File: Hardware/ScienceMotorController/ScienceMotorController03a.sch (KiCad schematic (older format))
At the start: 16 parts

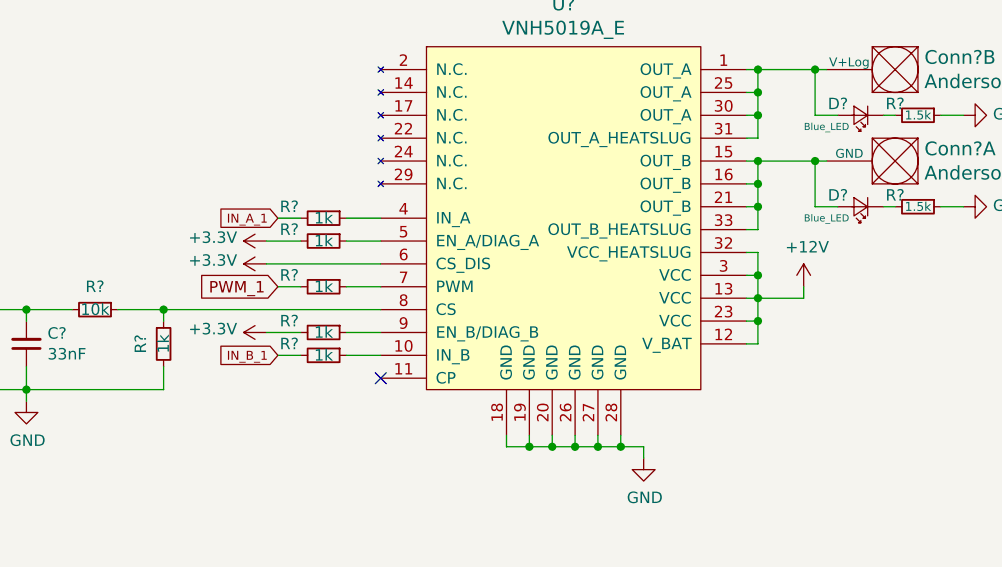
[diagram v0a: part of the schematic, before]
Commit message: changed everything to actuation, added schottky diode, added A/B flags to tiva
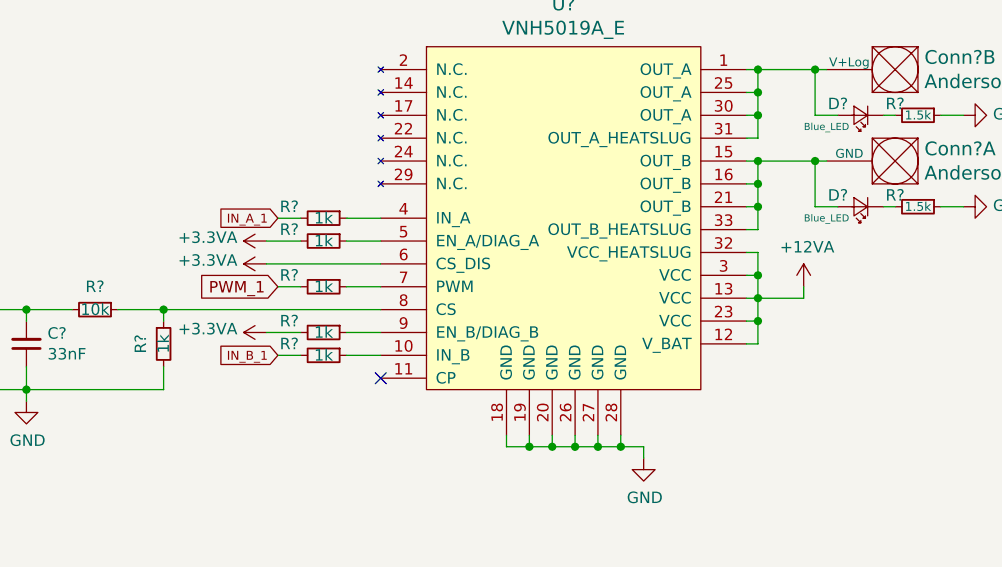
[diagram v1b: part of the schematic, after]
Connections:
- net +12V renamed +12VA
- net +3V3 renamed +3.3VA
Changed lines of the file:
@@
 	6700 3950 6700 3850
 Connection ~ 6700 3850
-$Comp
-L power:+12V #PWR?
-U 1 1 5FA34875
-P 6900 3700
-AR Path="/5F7D111E/5FA34875" Ref="#PWR?"  Part="1"
-AR Path="/5F7D111E/5FA0F855/5FA34875" Ref="#PWR?"  Part="1"
-F 0 "#PWR?" H 6900 3550 50  0001 C CNN
-F 1 "+12V" H 6915 3873 50  0000 C CNN
-F 2 "" H 6900 3700 50  0001 C CNN
-F 3 "" H 6900 3700 50  0001 C CNN
-	1    6900 3700
-	1    0    0    -1
-$EndComp
 Wire Wire Line
 	6900 3700 6900 3750
@@
 Wire Wire Line
 	4700 3900 4550 3900
-$Comp
-L power:+3.3V #PWR?
-U 1 1 5FA348B6
-P 4550 3900
-AR Path="/5F7D111E/5FA348B6" Ref="#PWR?"  Part="1"
-AR Path="/5F7D111E/5FA0F855/5FA348B6" Ref="#PWR?"  Part="1"
-F 0 "#PWR?" H 4550 3750 50  0001 C CNN
-F 1 "+3.3V" V 4565 4028 50  0000 L CNN
-F 2 "" H 4550 3900 50  0001 C CNN
-F 3 "" H 4550 3900 50  0001 C CNN
-	1    4550 3900
-	0    -1   -1   0
-$EndComp
-$Comp
-L power:+3.3V #PWR?
-U 1 1 5FA348BC
-P 4550 3600
-AR Path="/5F7D111E/5FA348BC" Ref="#PWR?"  Part="1"
-AR Path="/5F7D111E/5FA0F855/5FA348BC" Ref="#PWR?"  Part="1"
-F 0 "#PWR?" H 4550 3450 50  0001 C CNN
-F 1 "+3.3V" V 4565 3728 50  0000 L CNN
-F 2 "" H 4550 3600 50  0001 C CNN
-F 3 "" H 4550 3600 50  0001 C CNN
-	1    4550 3600
-	0    -1   -1   0
-$EndComp
 Wire Wire Line
 	5050 3600 4550 3600
@@
 Wire Wire Line
 	5050 3500 4900 3500
-$Comp
-L power:+3.3V #PWR?
-U 1 1 5FA348CA
-P 4550 3500
-AR Path="/5F7D111E/5FA348CA" Ref="#PWR?"  Part="1"
-AR Path="/5F7D111E/5FA0F855/5FA348CA" Ref="#PWR?"  Part="1"
-F 0 "#PWR?" H 4550 3350 50  0001 C CNN
-F 1 "+3.3V" V 4565 3628 50  0000 L CNN
-F 2 "" H 4550 3500 50  0001 C CNN
-F 3 "" H 4550 3500 50  0001 C CNN
-	1    4550 3500
-	0    -1   -1   0
-$EndComp
 Wire Wire Line
 	4700 3500 4550 3500
@@
 Text Notes 7150 6950 0    197  ~ 0
 Sheet 03a: Motor Driver 1
+$Comp
+L power:+3.3VA #PWR?
+U 1 1 5F82A3C3
+P 4550 3500
+F 0 "#PWR?" H 4550 3350 50  0001 C CNN
+F 1 "+3.3VA" V 4565 3627 50  0000 L CNN
+F 2 "" H 4550 3500 50  0001 C CNN
+F 3 "" H 4550 3500 50  0001 C CNN
+	1    4550 3500
+	0    -1   -1   0
+$EndComp
+$Comp
+L power:+3.3VA #PWR?
+U 1 1 5F82BB9F
+P 4550 3600
+F 0 "#PWR?" H 4550 3450 50  0001 C CNN
+F 1 "+3.3VA" V 4565 3727 50  0000 L CNN
+F 2 "" H 4550 3600 50  0001 C CNN
+F 3 "" H 4550 3600 50  0001 C CNN
+	1    4550 3600
+	0    -1   -1   0
+$EndComp
+$Comp
+L power:+3.3VA #PWR?
+U 1 1 5F82BED6
+P 4550 3900
+F 0 "#PWR?" H 4550 3750 50  0001 C CNN
+F 1 "+3.3VA" V 4565 4027 50  0000 L CNN
+F 2 "" H 4550 3900 50  0001 C CNN
+F 3 "" H 4550 3900 50  0001 C CNN
+	1    4550 3900
+	0    -1   -1   0
+$EndComp
+$Comp
+L power:+12VA #PWR?
+U 1 1 5F82C8B2
+P 6900 3700
+F 0 "#PWR?" H 6900 3550 50  0001 C CNN
+F 1 "+12VA" H 6915 3873 50  0000 C CNN
+F 2 "" H 6900 3700 50  0001 C CNN
+F 3 "" H 6900 3700 50  0001 C CNN
+	1    6900 3700
+	1    0    0    -1
+$EndComp
 $EndSCHEMATC

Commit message: fixed hierarchical
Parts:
- added FB? (x2): Ferrite_Bead, symbol Device:Ferrite_Bead_Small
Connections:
- net at U?.1 (OUT_A), U?.25 (OUT_A), U?.30 (OUT_A)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: now also FB?.2; no longer Conn?.2 (V+Log), D?.2 (A)
- net at U?.15 (OUT_B), U?.16 (OUT_B), U?.21 (OUT_B)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: now also FB?.2; no longer Conn?.1 (GND), D?.2 (A)
- net IN_A_1 renamed In_A_1
- net IN_B_1 renamed In_B_1
- new net: Conn?.2 (V+Log), D?.2 (A), FB?.1
- new net: Conn?.1 (GND), D?.2 (A), FB?.1
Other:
- moved on the sheet: Conn?A, Conn?B, D?, R?

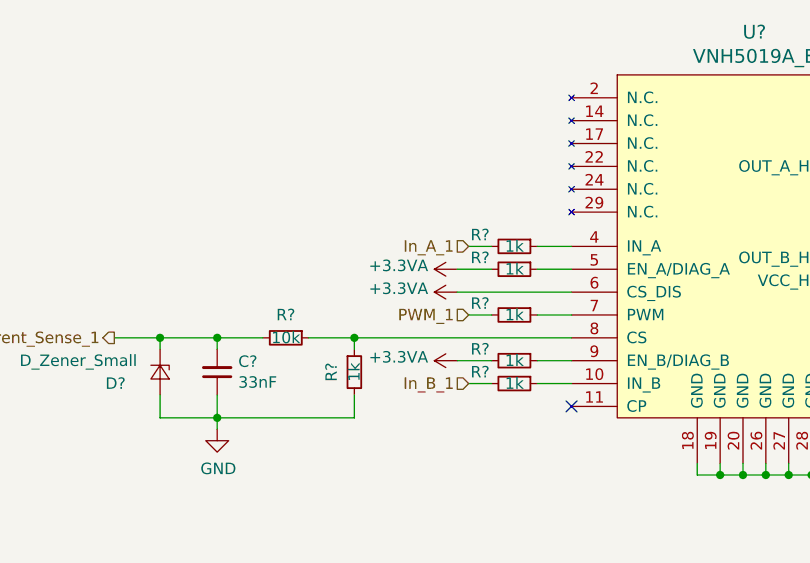
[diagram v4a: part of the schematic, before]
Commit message: Fixed 3.3V, added encoders
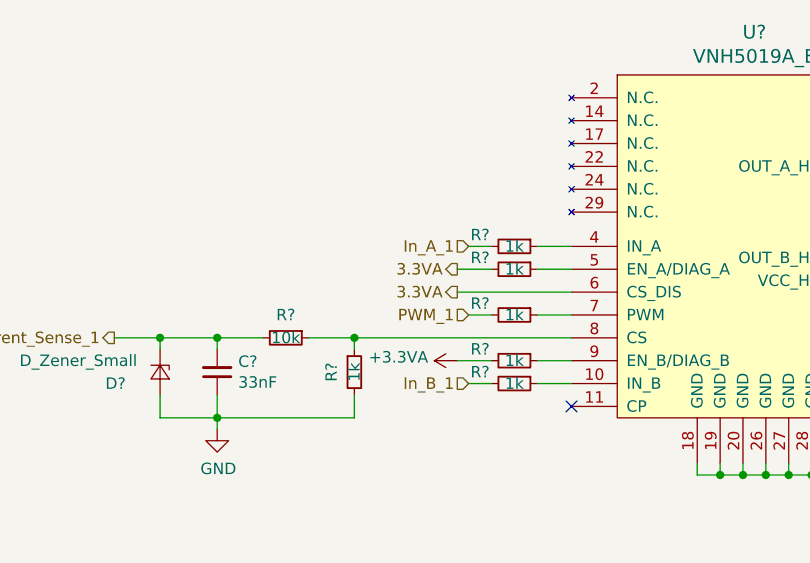
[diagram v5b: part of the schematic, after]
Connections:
- net +3.3VA: no longer R?.2, U?.6 (CS_DIS)
- new net 3.3VA: R?.2, U?.6 (CS_DIS)
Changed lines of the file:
@@
 $Descr A4 11693 8268
 encoding utf-8
-Sheet 10 10
+Sheet 10 11
 Title ""
 Date ""
@@
 $Comp
 L power:+3.3VA #PWR?
-U 1 1 5F82A3C3
-P 4550 3500
-AR Path="/5F7D111E/5FA0F855/5F82A3C3" Ref="#PWR?"  Part="1"
-AR Path="/5F9082F6/5F82A3C3" Ref="#PWR?"  Part="1"
-AR Path="/5F7148FA/5FA34AD3/5F82A3C3" Ref="#PWR?"  Part="1"
-F 0 "#PWR?" H 4550 3350 50  0001 C CNN
-F 1 "+3.3VA" V 4565 3627 50  0000 L CNN
-F 2 "" H 4550 3500 50  0001 C CNN
-F 3 "" H 4550 3500 50  0001 C CNN
-	1    4550 3500
-	0    -1   -1   0
-$EndComp
-$Comp
-L power:+3.3VA #PWR?
-U 1 1 5F82BB9F
-P 4550 3600
-AR Path="/5F7D111E/5FA0F855/5F82BB9F" Ref="#PWR?"  Part="1"
-AR Path="/5F9082F6/5F82BB9F" Ref="#PWR?"  Part="1"
-AR Path="/5F7148FA/5FA34AD3/5F82BB9F" Ref="#PWR?"  Part="1"
-F 0 "#PWR?" H 4550 3450 50  0001 C CNN
-F 1 "+3.3VA" V 4565 3727 50  0000 L CNN
-F 2 "" H 4550 3600 50  0001 C CNN
-F 3 "" H 4550 3600 50  0001 C CNN
-	1    4550 3600
-	0    -1   -1   0
-$EndComp
-$Comp
-L power:+3.3VA #PWR?
 U 1 1 5F82BED6
 P 4550 3900
@@
 Text HLabel 3050 3800 0    50   Output ~ 0
 Current_Sense_1
+Text HLabel 4550 3500 0    50   Output ~ 0
+3.3VA
+Text HLabel 4550 3600 0    50   Output ~ 0
+3.3VA
 $EndSCHEMATC

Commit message: added logic line
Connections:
- net 3.3VA is gone; now on net 3.3V: R?.2, U?.6 (CS_DIS)
- net +3.3VA renamed 3.3V
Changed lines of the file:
@@
 Sheet 03a: Motor Driver 1
-$Comp
-L power:+3.3VA #PWR?
-U 1 1 5F82BED6
-P 4550 3900
-AR Path="/5F7D111E/5FA0F855/5F82BED6" Ref="#PWR?"  Part="1"
-AR Path="/5F9082F6/5F82BED6" Ref="#PWR?"  Part="1"
-AR Path="/5F7148FA/5FA34AD3/5F82BED6" Ref="#PWR?"  Part="1"
-F 0 "#PWR?" H 4550 3750 50  0001 C CNN
-F 1 "+3.3VA" V 4565 4027 50  0000 L CNN
-F 2 "" H 4550 3900 50  0001 C CNN
-F 3 "" H 4550 3900 50  0001 C CNN
-	1    4550 3900
-	0    -1   -1   0
-$EndComp
 $Comp
 L power:+12VA #PWR?
@@
 Current_Sense_1
 Text HLabel 4550 3500 0    50   Output ~ 0
-3.3VA
+3.3V
 Text HLabel 4550 3600 0    50   Output ~ 0
-3.3VA
+3.3V
+Text HLabel 4550 3900 0    50   Output ~ 0
+3.3V
 $EndSCHEMATC

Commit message: annotated
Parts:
- C8: renamed from C?; footprint (none) -> Capacitor_SMD:C_0603_1608Metric_Pad1.05x0.95mm_HandSolder
- gave numbers to parts that had none: 16
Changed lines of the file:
@@
 AR Path="/5F7D111E/5FA0F855/5FA34863" Ref="U?"  Part="1"
 AR Path="/5F9082F6/5FA34863" Ref="U?"  Part="1"
-AR Path="/5F7148FA/5FA34AD3/5FA34863" Ref="U?"  Part="1"
-F 0 "U?" H 5850 5837 60  0000 C CNN
+AR Path="/5F7148FA/5FA34AD3/5FA34863" Ref="U8"  Part="1"
+F 0 "U8" H 5850 5837 60  0000 C CNN
 F 1 "VNH5019A_E" H 5850 5731 60  0000 C CNN
 F 2 "" H 5250 5450 60  0001 C CNN
@@
 AR Path="/5F7D111E/5FA0F855/5FA34880" Ref="R?"  Part="1"
 AR Path="/5F9082F6/5FA34880" Ref="R?"  Part="1"
-AR Path="/5F7148FA/5FA34AD3/5FA34880" Ref="R?"  Part="1"
-F 0 "R?" V 4750 3550 50  0000 C CNN
+AR Path="/5F7148FA/5FA34AD3/5FA34880" Ref="R59"  Part="1"
+F 0 "R59" V 4750 3550 50  0000 C CNN
 F 1 "1k" V 4800 3700 50  0000 C CNN
 F 2 "" H 4800 3700 50  0001 C CNN
@@
 AR Path="/5F7D111E/5FA0F855/5FA34886" Ref="R?"  Part="1"
 AR Path="/5F9082F6/5FA34886" Ref="R?"  Part="1"
-AR Path="/5F7148FA/5FA34AD3/5FA34886" Ref="R?"  Part="1"
-F 0 "R?" V 4000 3950 50  0000 C CNN
+AR Path="/5F7148FA/5FA34AD3/5FA34886" Ref="R56"  Part="1"
+F 0 "R56" V 4000 3950 50  0000 C CNN
 F 1 "1k" V 4100 3950 50  0000 C CNN
 F 2 "" H 4100 3950 50  0001 C CNN
@@
 AR Path="/5F7D111E/5FA0F855/5FA3488C" Ref="C?"  Part="1"
 AR Path="/5F9082F6/5FA3488C" Ref="C?"  Part="1"
-AR Path="/5F7148FA/5FA34AD3/5FA3488C" Ref="C?"  Part="1"
-F 0 "C?" H 3408 3904 50  0000 R CNN
+AR Path="/5F7148FA/5FA34AD3/5FA3488C" Ref="C8"  Part="1"
+F 0 "C8" H 3408 3904 50  0000 R CNN
 F 1 "33nF" H 3408 3995 50  0000 R CNN
-F 2 "" H 3500 3950 50  0001 C CNN
+F 2 "Capacitor_SMD:C_0603_1608Metric_Pad1.05x0.95mm_HandSolder" H 3500 3950 50  0001 C CNN
 F 3 "~" H 3500 3950 50  0001 C CNN
 	1    3500 3950
@@
 AR Path="/5F7D111E/5FA0F855/5FA34892" Ref="D?"  Part="1"
 AR Path="/5F9082F6/5FA34892" Ref="D?"  Part="1"
-AR Path="/5F7148FA/5FA34AD3/5FA34892" Ref="D?"  Part="1"
-F 0 "D?" V 3300 3800 50  0000 R CNN
+AR Path="/5F7148FA/5FA34AD3/5FA34892" Ref="D26"  Part="1"
+F 0 "D26" V 3300 3800 50  0000 R CNN
 F 1 "D_Zener_Small" V 3200 3850 50  0000 R CNN
 F 2 "" V 3250 3950 50  0001 C CNN
@@
 AR Path="/5F7D111E/5FA0F855/5FA34898" Ref="R?"  Part="1"
 AR Path="/5F9082F6/5FA34898" Ref="R?"  Part="1"
-AR Path="/5F7148FA/5FA34AD3/5FA34898" Ref="R?"  Part="1"
-F 0 "R?" V 3700 3800 50  0000 C CNN
+AR Path="/5F7148FA/5FA34AD3/5FA34898" Ref="R55"  Part="1"
+F 0 "R55" V 3700 3800 50  0000 C CNN
 F 1 "10k" V 3800 3800 50  0000 C CNN
 F 2 "" H 3800 3800 50  0001 C CNN
@@
 AR Path="/5F7D111E/5FA0F855/5FA348AE" Ref="R?"  Part="1"
 AR Path="/5F9082F6/5FA348AE" Ref="R?"  Part="1"
-AR Path="/5F7148FA/5FA34AD3/5FA348AE" Ref="R?"  Part="1"
-F 0 "R?" V 4750 3750 50  0000 C CNN
+AR Path="/5F7148FA/5FA34AD3/5FA348AE" Ref="R60"  Part="1"
+F 0 "R60" V 4750 3750 50  0000 C CNN
 F 1 "1k" V 4800 3900 50  0000 C CNN
 F 2 "" H 4800 3900 50  0001 C CNN
@@
 AR Path="/5F7D111E/5FA0F855/5FA348C3" Ref="R?"  Part="1"
 AR Path="/5F9082F6/5FA348C3" Ref="R?"  Part="1"
-AR Path="/5F7148FA/5FA34AD3/5FA348C3" Ref="R?"  Part="1"
-F 0 "R?" V 4750 3350 50  0000 C CNN
+AR Path="/5F7148FA/5FA34AD3/5FA348C3" Ref="R58"  Part="1"
+F 0 "R58" V 4750 3350 50  0000 C CNN
 F 1 "1k" V 4800 3500 50  0000 C CNN
 F 2 "" H 4800 3500 50  0001 C CNN
@@
 AR Path="/5F7D111E/5FA0F855/5FA348D1" Ref="R?"  Part="1"
 AR Path="/5F9082F6/5FA348D1" Ref="R?"  Part="1"
-AR Path="/5F7148FA/5FA34AD3/5FA348D1" Ref="R?"  Part="1"
-F 0 "R?" V 4750 3250 50  0000 C CNN
+AR Path="/5F7148FA/5FA34AD3/5FA348D1" Ref="R57"  Part="1"
+F 0 "R57" V 4750 3250 50  0000 C CNN
 F 1 "1k" V 4800 3400 50  0000 C CNN
 F 2 "" H 4800 3400 50  0001 C CNN
@@
 AR Path="/5F7D111E/5FA0F855/5FA348DB" Ref="R?"  Part="1"
 AR Path="/5F9082F6/5FA348DB" Ref="R?"  Part="1"
-AR Path="/5F7148FA/5FA34AD3/5FA348DB" Ref="R?"  Part="1"
-F 0 "R?" V 4750 3850 50  0000 C CNN
+AR Path="/5F7148FA/5FA34AD3/5FA348DB" Ref="R61"  Part="1"
+F 0 "R61" V 4750 3850 50  0000 C CNN
 F 1 "1k" V 4800 4000 50  0000 C CNN
 F 2 "" H 4800 4000 50  0001 C CNN
@@
 AR Path="/5F7D111E/5FA0F855/5FA348F3" Ref="#PWR?"  Part="1"
 AR Path="/5F9082F6/5FA348F3" Ref="#PWR?"  Part="1"
-AR Path="/5F7148FA/5FA34AD3/5FA348F3" Ref="#PWR?"  Part="1"
-F 0 "#PWR?" H 6200 4200 50  0001 C CNN
+AR Path="/5F7148FA/5FA34AD3/5FA348F3" Ref="#PWR046"  Part="1"
+F 0 "#PWR046" H 6200 4200 50  0001 C CNN
 F 1 "GND" H 6205 4277 50  0000 C CNN
 F 2 "" H 6200 4450 50  0001 C CNN
@@
 AR Path="/5F7D111E/5FA0F855/5FA348FD" Ref="#PWR?"  Part="1"
 AR Path="/5F9082F6/5FA348FD" Ref="#PWR?"  Part="1"
-AR Path="/5F7148FA/5FA34AD3/5FA348FD" Ref="#PWR?"  Part="1"
-F 0 "#PWR?" H 3500 3950 50  0001 C CNN
+AR Path="/5F7148FA/5FA34AD3/5FA348FD" Ref="#PWR045"  Part="1"
+F 0 "#PWR045" H 3500 3950 50  0001 C CNN
 F 1 "GND" H 3505 4027 50  0000 C CNN
 F 2 "" H 3500 4200 50  0001 C CNN
@@
 AR Path="/5F7D111E/5FA0F855/5FA34915" Ref="Conn?"  Part="1"
 AR Path="/5F9082F6/5FA34915" Ref="Conn?"  Part="1"
-AR Path="/5F7148FA/5FA34AD3/5FA34915" Ref="Conn?"  Part="1"
-F 0 "Conn?" H 7772 3097 60  0000 R CNN
+AR Path="/5F7148FA/5FA34AD3/5FA34915" Ref="Conn11"  Part="1"
+F 0 "Conn11" H 7772 3097 60  0000 R CNN
 F 1 "AndersonPP" H 7772 3203 60  0000 R CNN
 F 2 "" H 7650 2500 60  0001 C CNN
@@
 AR Path="/5F7D111E/5FA0F855/5FA3491B" Ref="Conn?"  Part="2"
 AR Path="/5F9082F6/5FA3491B" Ref="Conn?"  Part="2"
-AR Path="/5F7148FA/5FA34AD3/5FA3491B" Ref="Conn?"  Part="2"
-F 0 "Conn?" H 7772 2697 60  0000 R CNN
+AR Path="/5F7148FA/5FA34AD3/5FA3491B" Ref="Conn11"  Part="2"
+F 0 "Conn11" H 7772 2697 60  0000 R CNN
 F 1 "AndersonPP" H 7772 2803 60  0000 R CNN
 F 2 "" H 7650 2100 60  0001 C CNN
@@
 AR Path="/5F7D111E/5FA0F855/5FA3492F" Ref="D?"  Part="1"
 AR Path="/5F9082F6/5FA3492F" Ref="D?"  Part="1"
-AR Path="/5F7148FA/5FA34AD3/5FA3492F" Ref="D?"  Part="1"
-F 0 "D?" H 7650 2900 50  0000 C CNN
+AR Path="/5F7148FA/5FA34AD3/5FA3492F" Ref="D27"  Part="1"
+F 0 "D27" H 7650 2900 50  0000 C CNN
 F 1 "Blue_LED" H 7700 3000 31  0000 C CNN
 F 2 "" V 7550 2950 50  0001 C CNN
@@
 AR Path="/5F7D111E/5FA0F855/5FA34935" Ref="D?"  Part="1"
 AR Path="/5F9082F6/5FA34935" Ref="D?"  Part="1"
-AR Path="/5F7148FA/5FA34AD3/5FA34935" Ref="D?"  Part="1"
-F 0 "D?" H 7650 3300 50  0000 C CNN
+AR Path="/5F7148FA/5FA34AD3/5FA34935" Ref="D28"  Part="1"
+F 0 "D28" H 7650 3300 50  0000 C CNN
 F 1 "Blue_LED" H 7700 3400 31  0000 C CNN
 F 2 "" V 7550 3350 50  0001 C CNN
@@
 AR Path="/5F7D111E/5FA0F855/5FA3493B" Ref="R?"  Part="1"
 AR Path="/5F9082F6/5FA3493B" Ref="R?"  Part="1"
-AR Path="/5F7148FA/5FA34AD3/5FA3493B" Ref="R?"  Part="1"
-F 0 "R?" V 7750 3250 50  0000 C CNN
+AR Path="/5F7148FA/5FA34AD3/5FA3493B" Ref="R63"  Part="1"
+F 0 "R63" V 7750 3250 50  0000 C CNN
 F 1 "1.5k" V 7800 3350 39  0000 C CNN
 F 2 "" H 7800 3350 50  0001 C CNN
@@
 AR Path="/5F7D111E/5FA0F855/5FA34941" Ref="R?"  Part="1"
 AR Path="/5F9082F6/5FA34941" Ref="R?"  Part="1"
-AR Path="/5F7148FA/5FA34AD3/5FA34941" Ref="R?"  Part="1"
-F 0 "R?" V 7750 2850 50  0000 C CNN
+AR Path="/5F7148FA/5FA34AD3/5FA34941" Ref="R62"  Part="1"
+F 0 "R62" V 7750 2850 50  0000 C CNN
 F 1 "1.5k" V 7800 2950 39  0000 C CNN
 F 2 "" H 7800 2950 50  0001 C CNN
@@
 AR Path="/5F7D111E/5FA0F855/5FA34949" Ref="#PWR?"  Part="1"
 AR Path="/5F9082F6/5FA34949" Ref="#PWR?"  Part="1"
-AR Path="/5F7148FA/5FA34AD3/5FA34949" Ref="#PWR?"  Part="1"
-F 0 "#PWR?" H 8000 2700 50  0001 C CNN
+AR Path="/5F7148FA/5FA34AD3/5FA34949" Ref="#PWR048"  Part="1"
+F 0 "#PWR048" H 8000 2700 50  0001 C CNN
 F 1 "GND" V 8005 2822 50  0000 R CNN
 F 2 "" H 8000 2950 50  0001 C CNN
@@
 AR Path="/5F7D111E/5FA0F855/5FA3494F" Ref="#PWR?"  Part="1"
 AR Path="/5F9082F6/5FA3494F" Ref="#PWR?"  Part="1"
-AR Path="/5F7148FA/5FA34AD3/5FA3494F" Ref="#PWR?"  Part="1"
-F 0 "#PWR?" H 8000 3100 50  0001 C CNN
+AR Path="/5F7148FA/5FA34AD3/5FA3494F" Ref="#PWR049"  Part="1"
+F 0 "#PWR049" H 8000 3100 50  0001 C CNN
 F 1 "GND" V 8005 3222 50  0000 R CNN
 F 2 "" H 8000 3350 50  0001 C CNN
@@
 AR Path="/5F7D111E/5FA0F855/5F82C8B2" Ref="#PWR?"  Part="1"
 AR Path="/5F9082F6/5F82C8B2" Ref="#PWR?"  Part="1"
-AR Path="/5F7148FA/5FA34AD3/5F82C8B2" Ref="#PWR?"  Part="1"
-F 0 "#PWR?" H 6900 3550 50  0001 C CNN
+AR Path="/5F7148FA/5FA34AD3/5F82C8B2" Ref="#PWR047"  Part="1"
+F 0 "#PWR047" H 6900 3550 50  0001 C CNN
 F 1 "+12VA" H 6915 3873 50  0000 C CNN
 F 2 "" H 6900 3700 50  0001 C CNN
@@
 P 7000 2750
 AR Path="/5F9082F6/5F9C1894" Ref="FB?"  Part="1"
-AR Path="/5F7148FA/5FA34AD3/5F9C1894" Ref="FB?"  Part="1"
-F 0 "FB?" V 6763 2750 50  0000 C CNN
+AR Path="/5F7148FA/5FA34AD3/5F9C1894" Ref="FB11"  Part="1"
+F 0 "FB11" V 6763 2750 50  0000 C CNN
 F 1 "Ferrite_Bead" V 6854 2750 50  0000 C CNN
 F 2 "" V 6930 2750 50  0001 C CNN
@@
 P 7000 3150
 AR Path="/5F9082F6/5F9C2846" Ref="FB?"  Part="1"
-AR Path="/5F7148FA/5FA34AD3/5F9C2846" Ref="FB?"  Part="1"
-F 0 "FB?" V 6850 3150 50  0000 C CNN
+AR Path="/5F7148FA/5FA34AD3/5F9C2846" Ref="FB12"  Part="1"
+F 0 "FB12" V 6850 3150 50  0000 C CNN
 F 1 "Ferrite_Bead" V 6900 3150 50  0000 C CNN
 F 2 "" V 6930 3150 50  0001 C CNN
